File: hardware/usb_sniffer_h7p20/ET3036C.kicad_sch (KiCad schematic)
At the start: 27 parts, among them U11 EA3036C

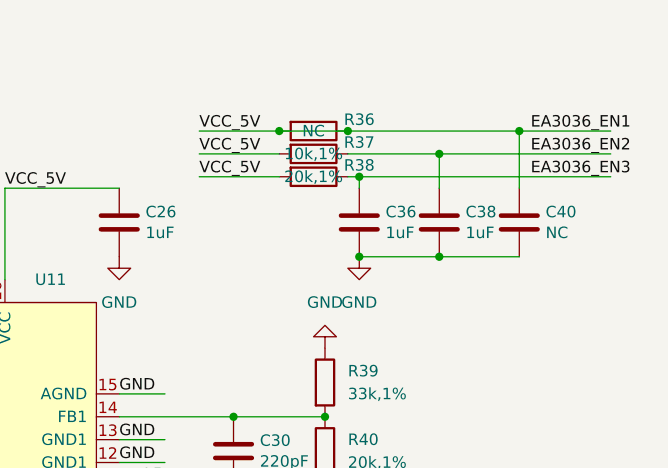
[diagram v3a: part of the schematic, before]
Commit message: [usb_sniffer_h7p20]增加JTAG排针，增加产品页二维码
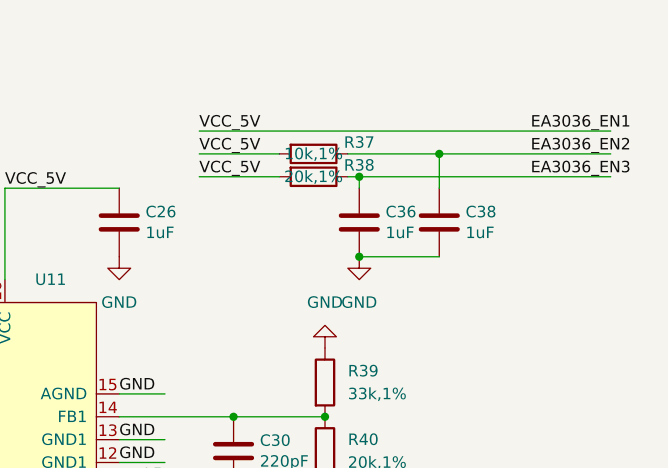
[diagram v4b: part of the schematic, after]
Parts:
- removed C40: NC, Capacitor_SMD:C_0402_1005Metric, symbol Device:C
- removed R36: NC, Resistor_SMD:R_0402_1005Metric, symbol Device:R
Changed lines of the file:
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@@
   (junction (at 182.88 93.98) (diameter 0) (color 0 0 0 0)
   )
-  (junction (at 204.47 62.23) (diameter 0) (color 0 0 0 0)
-  )
-  (junction (at 185.42 62.23) (diameter 0) (color 0 0 0 0)
-  )
   (junction (at 172.72 93.98) (diameter 0) (color 0 0 0 0)
   )
@@
   (junction (at 111.76 88.9) (diameter 0) (color 0 0 0 0)
   )
-  (junction (at 177.8 62.23) (diameter 0) (color 0 0 0 0)
-  )
-  (junction (at 195.58 76.2) (diameter 0) (color 0 0 0 0)
-  )
   (junction (at 114.3 118.11) (diameter 0) (color 0 0 0 0)
   )
@@
     (stroke (width 0) (type default))
   )
-  (wire (pts (xy 168.91 62.23) (xy 177.8 62.23))
+  (wire (pts (xy 168.91 62.23) (xy 214.63 62.23))
     (stroke (width 0) (type default))
   )
@@
     (stroke (width 0) (type default))
   )
-  (wire (pts (xy 177.8 62.23) (xy 185.42 62.23))
-    (stroke (width 0) (type default))
-  )
   (wire (pts (xy 114.3 125.73) (xy 123.19 125.73))
     (stroke (width 0) (type default))
@@
     (stroke (width 0) (type default))
   )
-  (wire (pts (xy 204.47 68.58) (xy 204.47 62.23))
-    (stroke (width 0) (type default))
-  )
   (wire (pts (xy 182.88 101.6) (xy 191.77 101.6))
     (stroke (width 0) (type default))
@@
     (stroke (width 0) (type default))
   )
-  (wire (pts (xy 195.58 76.2) (xy 204.47 76.2))
-    (stroke (width 0) (type default))
-  )
   (wire (pts (xy 168.91 67.31) (xy 177.8 67.31))
     (stroke (width 0) (type default))
@@
     (stroke (width 0) (type default))
   )
-  (wire (pts (xy 204.47 62.23) (xy 214.63 62.23))
-    (stroke (width 0) (type default))
-  )
   (wire (pts (xy 160.02 96.52) (xy 165.1 96.52))
-    (stroke (width 0) (type default))
-  )
-  (wire (pts (xy 185.42 62.23) (xy 204.47 62.23))
     (stroke (width 0) (type default))
   )
@@
         )
       )
-    )
-  )
-  (symbol (lib_id "Device:C") (at 204.47 72.39 180) (unit 1)
-    (in_bom yes) (on_board yes) (dnp no)
-    (property "Reference" "C40" (at 207.391 71.2216 0)
-      (effects (font (size 1.27 1.27)) (justify right))
-    )
-    (property "Value" "NC" (at 207.391 73.533 0)
-      (effects (font (size 1.27 1.27)) (justify right))
-    )
-    (property "Footprint" "Capacitor_SMD:C_0402_1005Metric" (at 203.5048 68.58 0)
-      (effects (font (size 1.27 1.27)) hide)
-    )
-    (property "Datasheet" "~" (at 204.47 72.39 0)
-      (effects (font (size 1.27 1.27)) hide)
-    )
-    (pin "1")
-    (pin "2")
-    (instances
-      (project "usb_sniffer_h7p20"
-        (path "/5a8287a8-9f7a-4e60-a3bf-19c1227b20fe/47602f55-4b85-492b-8b27-513bc90aa2b6"
-          (reference "C40") (unit 1)
-        )
-      )
-    )
-  )
-  (symbol (lib_id "Device:R") (at 181.61 62.23 270) (unit 1)
-    (in_bom yes) (on_board yes) (dnp no)
-    (property "Reference" "R36" (at 186.69 60.96 90)
-      (effects (font (size 1.27 1.27)))
-    )
-    (property "Value" "NC" (at 181.61 62.23 90)
-      (effects (font (size 1.27 1.27)))
-    )
-    (property "Footprint" "Resistor_SMD:R_0402_1005Metric" (at 181.61 60.452 90)
-      (effects (font (size 1.27 1.27)) hide)
-    )
-    (property "Datasheet" "~" (at 181.61 62.23 0)
-      (effects (font (size 1.27 1.27)) hide)
-    )
-    (pin "1")
-    (pin "2")
-    (instances
-      (project "usb_sniffer_h7p20"
-        (path "/5a8287a8-9f7a-4e60-a3bf-19c1227b20fe/47602f55-4b85-492b-8b27-513bc90aa2b6"
-          (reference "R36") (unit 1)
-        )
-      )

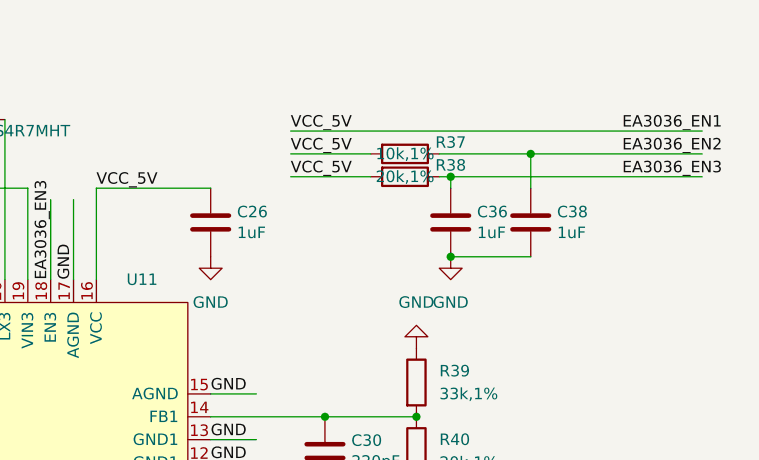
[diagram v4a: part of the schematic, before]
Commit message: [usb_sniffer_h7p20] 优化上电
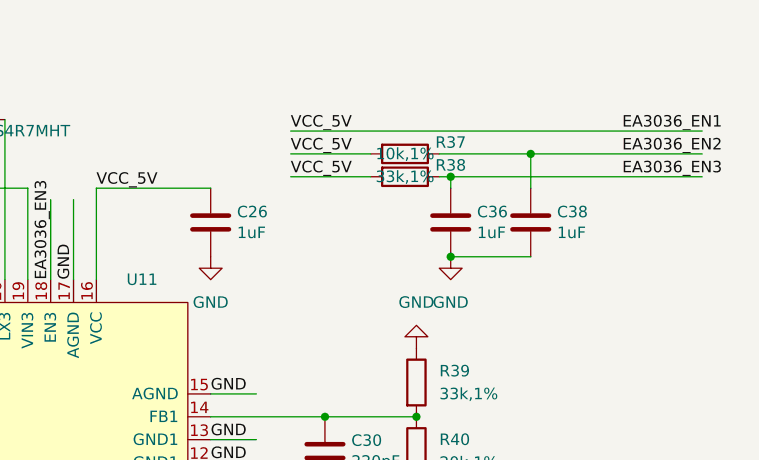
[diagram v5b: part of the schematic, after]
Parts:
- R38: value 20k,1% -> 33k,1%
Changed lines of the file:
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@@
       (effects (font (size 1.27 1.27)))
     )
-    (property "Value" "20k,1%" (at 181.61 67.31 90)
+    (property "Value" "33k,1%" (at 181.61 67.31 90)
       (effects (font (size 1.27 1.27)))
     )

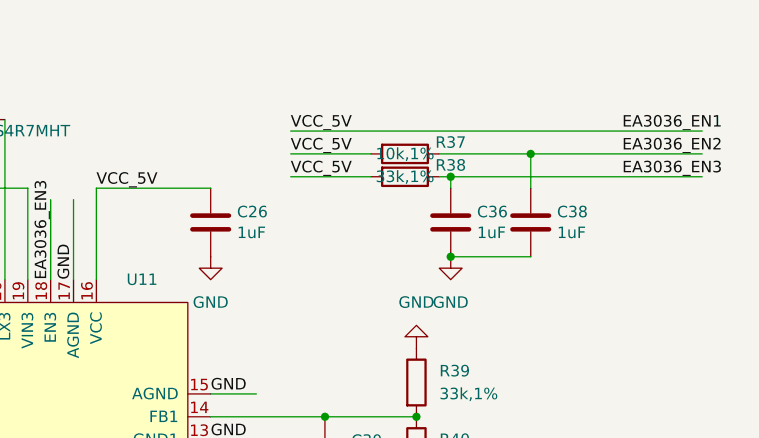
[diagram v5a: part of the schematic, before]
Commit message: [usb_sniffer_h7p20] 优化上电
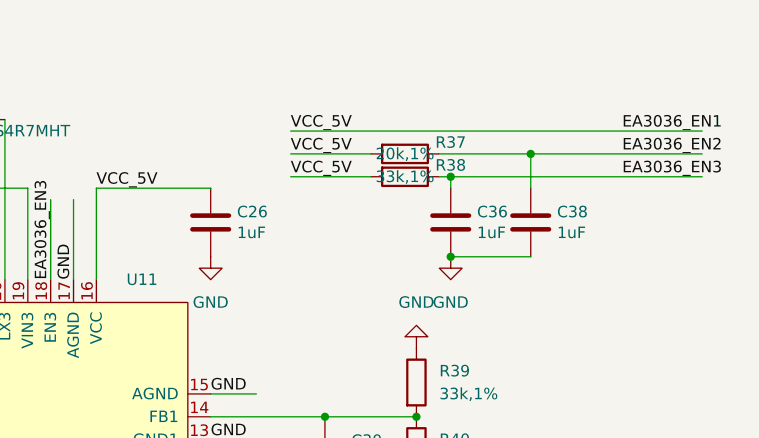
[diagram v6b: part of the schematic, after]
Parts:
- R37: value 10k,1% -> 20k,1%
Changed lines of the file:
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@@
       (effects (font (size 1.27 1.27)))
     )
-    (property "Value" "10k,1%" (at 181.61 64.77 90)
+    (property "Value" "20k,1%" (at 181.61 64.77 90)
       (effects (font (size 1.27 1.27)))
     )

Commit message: [usb_sniffer_h7p20] 适配铝合金外壳、更换CH132C
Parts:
- L5: footprint vllogic:L_NR3015 -> vllogic:L_NR2520xx
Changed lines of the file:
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@@
 			)
 		)
-		(property "Footprint" "vllogic:L_NR3015"
+		(property "Footprint" "vllogic:L_NR2520xx"
 			(at 168.91 101.6 0)
 			(effects
